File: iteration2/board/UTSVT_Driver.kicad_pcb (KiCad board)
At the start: 2 copper layers, 23 parts

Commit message: Generated netlist
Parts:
- added C1: C, Capacitors_SMD:C_0805_HandSoldering, F.Cu at (142.3, 2.73)
- added C2: 100nF, Capacitors_SMD:C_0805_HandSoldering, F.Cu at (151.3, 9.78)
- added C3: 100nF, Capacitors_SMD:C_0805_HandSoldering, F.Cu at (151.3, 25.8)
- added C4: 100nF, Capacitors_SMD:C_0805_HandSoldering, F.Cu at (151.3, 41.8)
- added C5: 100nF, Capacitors_SMD:C_0805_HandSoldering, F.Cu at (151.3, 50.7)
- added D1: BAV99, Diodes_SMD:D_0805, F.Cu at (162.6, 8.07)
- added D2: BAV99, Diodes_SMD:D_0805, F.Cu at (162.6, 24.1)
- added D3: BAV99, Diodes_SMD:D_0805, F.Cu at (162.6, 40.1)
- added D4: BAV99, Diodes_SMD:D_0805, F.Cu at (161.4, 50.6)
- added J1: DB37_Female_MountingHoles, Connectors_DSub:DB37FC, F.Cu at (9.22, 20.9)
- added Q1: 2N7002, TO_SOT_Packages_SMD:SOT-23, F.Cu at (151.9, 3.48)
- added Q2: 2N7002, TO_SOT_Packages_SMD:SOT-23, F.Cu at (151.9, 19.5)
- added Q3: 2N7002, TO_SOT_Packages_SMD:SOT-23, F.Cu at (151.9, 35.5)
- added R1: 10K, Resistors_SMD:R_0805_HandSoldering, F.Cu at (157.5, 8.18)
- added R10: 10K, Resistors_SMD:R_0805_HandSoldering, F.Cu at (151.3, 56.2)
- added R11: 1M, Resistors_SMD:R_0805_HandSoldering, F.Cu at (156.3, 50.7)
- added R2: 10K, Resistors_SMD:R_0805_HandSoldering, F.Cu at (162.7, 2.67)
- added R3: 10K, Resistors_SMD:R_0805_HandSoldering, F.Cu at (157.5, 2.67)
- added R4: 10K, Resistors_SMD:R_0805_HandSoldering, F.Cu at (157.5, 24.2)
- added R5: 10K, Resistors_SMD:R_0805_HandSoldering, F.Cu at (162.7, 18.7)
- added R6: 10K, Resistors_SMD:R_0805_HandSoldering, F.Cu at (157.5, 18.7)
- added R7: 10K, Resistors_SMD:R_0805_HandSoldering, F.Cu at (157.5, 34.7)
- added R8: 10K, Resistors_SMD:R_0805_HandSoldering, F.Cu at (162.7, 34.7)
- added R9: 10K, Resistors_SMD:R_0805_HandSoldering, F.Cu at (157.5, 40.2)
- added U1: Nucleo, UTSVT_board:AFBShieldBoard, F.Cu at (17.5, 53.4)
- added U2: SN65HVD230, Housings_SOIC:SOIC-8_3.9x4.9mm_Pitch1.27mm, F.Cu at (97.1, 57.3)
- added U3: CAN_adapter, UTSVT_board:CAN_adapter, F.Cu at (59.5, 31.8)
- moved REF** 111.0 mm to (7.50, 78.7)
- moved REF** 93.1 mm to (25.0, 78.7)
- moved REF** 78.9 mm to (57.7, 40.6)
- moved REF** 70.3 mm to (128.5, 17.4)
- moved REF** 65.9 mm to (57.7, 46.1)
- moved REF** 65.7 mm to (122.7, 22.8)
- moved REF** 64.0 mm to (122.7, 28.2)
- moved REF** 63.5 mm to (42.6, 78.7)
- moved REF** 63.4 mm to (57.7, 64.6)
- moved REF** 63.4 mm to (140.2, 17.3)
- moved REF** 62.1 mm to (128.7, 28.2)
- moved REF** 53.5 mm to (128.7, 22.8)
- moved REF** 52.3 mm to (57.7, 70.1)
- moved REF** 50.4 mm to (61.7, 57.3)
- moved REF** 49.2 mm to (130.3, 8.60)
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
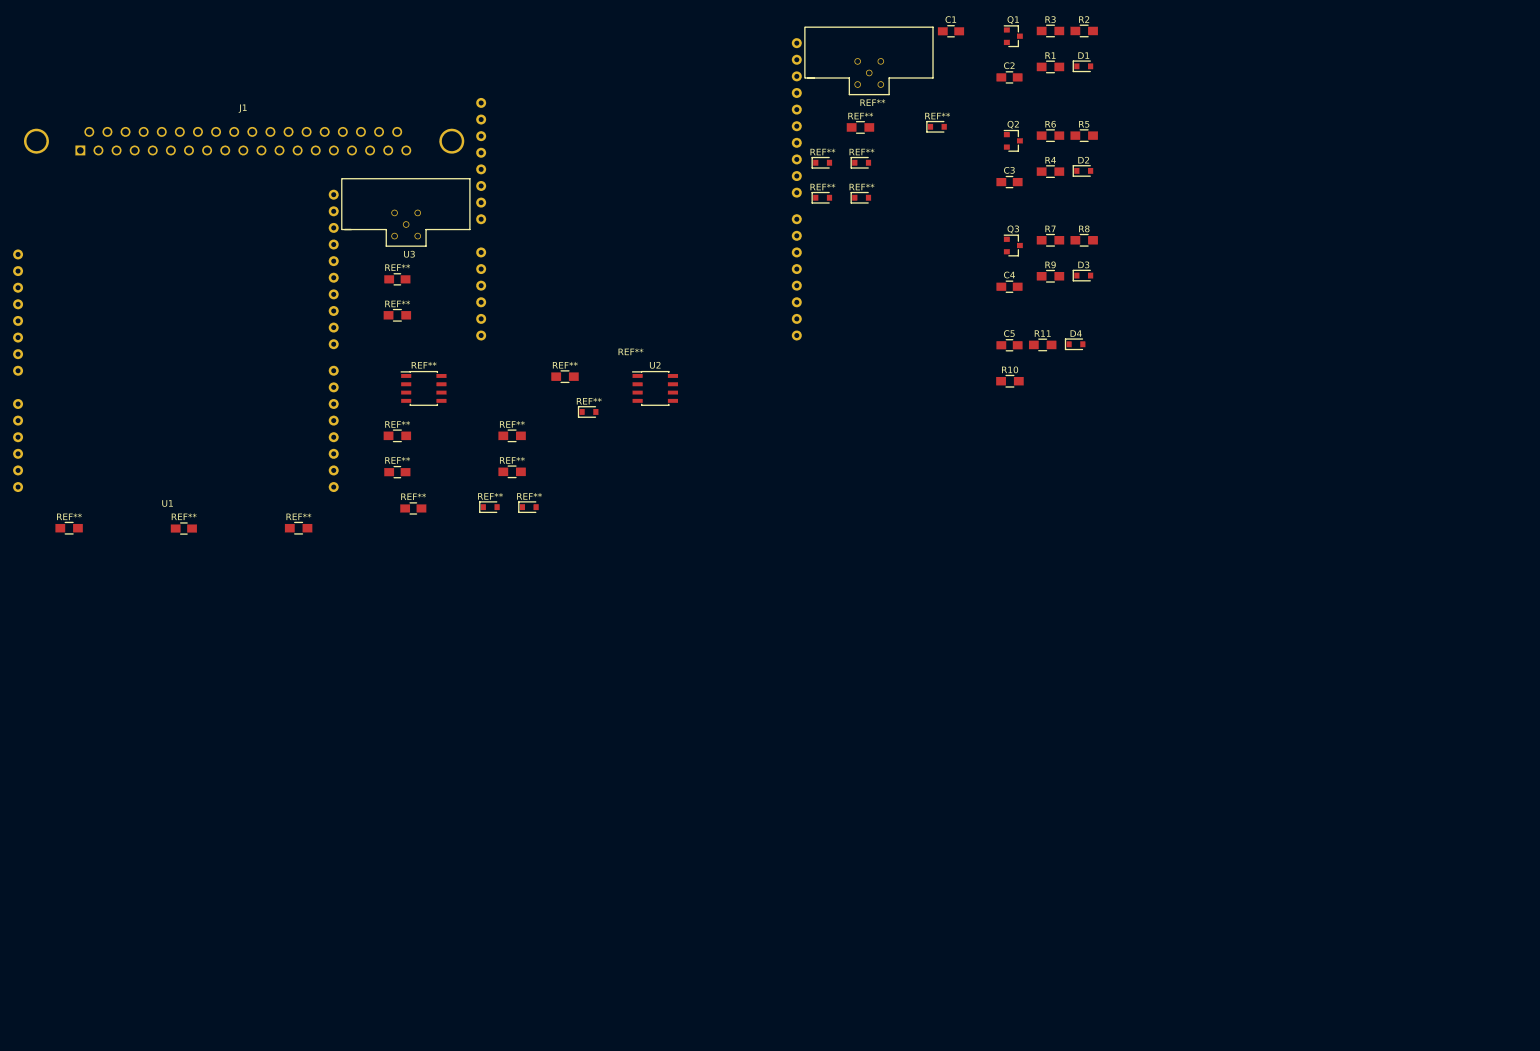
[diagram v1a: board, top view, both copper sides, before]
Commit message: Redid some components to fit footprint
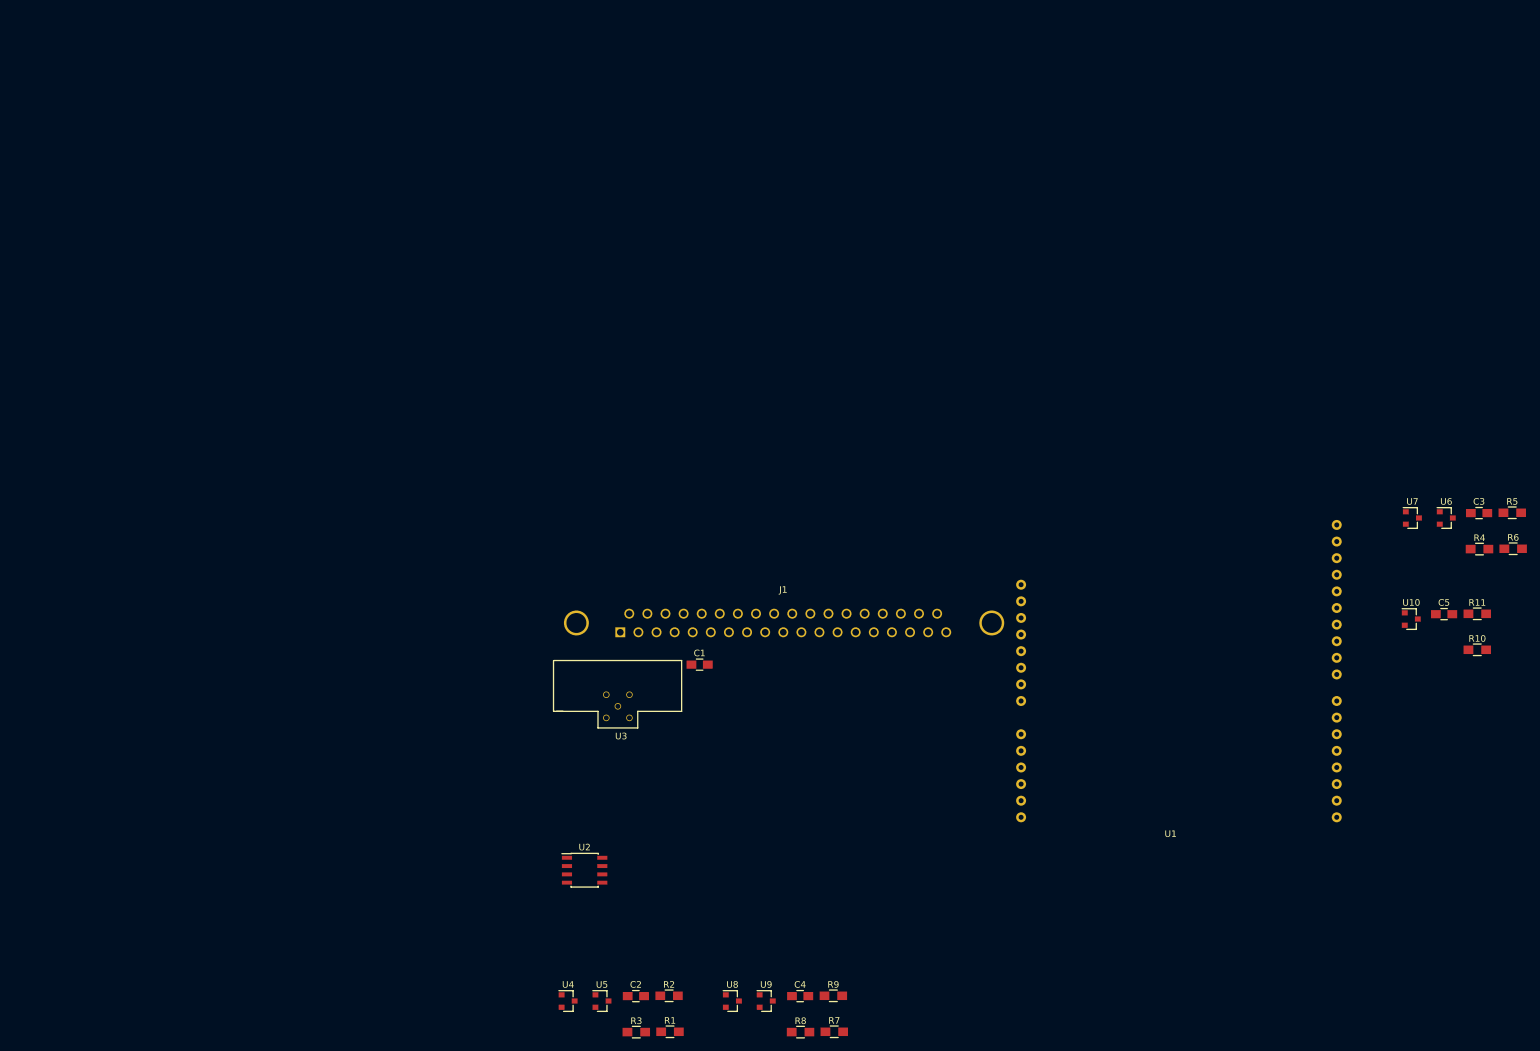
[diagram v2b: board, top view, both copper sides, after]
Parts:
- removed D1, D2, D3, D4: BAV99, Diodes_SMD:D_0805
- removed Q1, Q2, Q3: 2N7002, TO_SOT_Packages_SMD:SOT-23
- removed REF** (x8): R_0805_HandSoldering, Resistors_SMD:R_0805_HandSoldering
- removed REF** (x8): D_0805, Diodes_SMD:D_0805
- removed REF** (x4): C_0805_HandSoldering, Capacitors_SMD:C_0805_HandSoldering
- removed REF**: CANadapter, MotorControllerStuff:CANadapter
- removed REF**: SOIC-8_3.9x4.9mm_Pitch1.27mm, Housings_SOIC:SOIC-8_3.9x4.9mm_Pitch1.27mm
- removed REF**: AFBShield Board, MotorControllerStuff:AFBShieldBoard
- added U10: BAV99, TO_SOT_Packages_SMD:SOT-23, F.Cu at (212.7, 92.6)
- added U4: BAV99, TO_SOT_Packages_SMD:SOT-23, F.Cu at (83.8, 151.0)
- added U5: MOS_N, TO_SOT_Packages_SMD:SOT-23, F.Cu at (89.0, 151.0)
- added U6: BAV99, TO_SOT_Packages_SMD:SOT-23, F.Cu at (218.0, 77.1)
- added U7: MOS_N, TO_SOT_Packages_SMD:SOT-23, F.Cu at (212.9, 77.1)
- added U8: BAV99, TO_SOT_Packages_SMD:SOT-23, F.Cu at (108.9, 151.0)
- added U9: MOS_N, TO_SOT_Packages_SMD:SOT-23, F.Cu at (114.1, 151.0)
- J1: footprint Connectors_DSub:DB37FC -> UTSVT_board:DB37FC
- moved R3 165.6 mm to (94.2, 155.7)
- moved U1 161.4 mm to (170.8, 103.8)
- moved R2 160.6 mm to (99.2, 150.2)
- moved R1 158.6 mm to (99.4, 155.7)
- moved C2 151.6 mm to (94.1, 150.2)
- moved R8 128.6 mm to (119.3, 155.7)
- moved R7 125.4 mm to (124.5, 155.7)
- moved R9 114.9 mm to (124.3, 150.2)
- moved C4 113.1 mm to (119.3, 150.2)
- moved J1 110.6 mm to (91.8, 94.6)
- moved C1 104.2 mm to (103.9, 99.6)
- moved R6 94.8 mm to (228.3, 81.8)
- moved C3 87.8 mm to (223.1, 76.4)
- moved R4 87.4 mm to (223.1, 81.9)
- moved R5 87.2 mm to (228.1, 76.3)
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
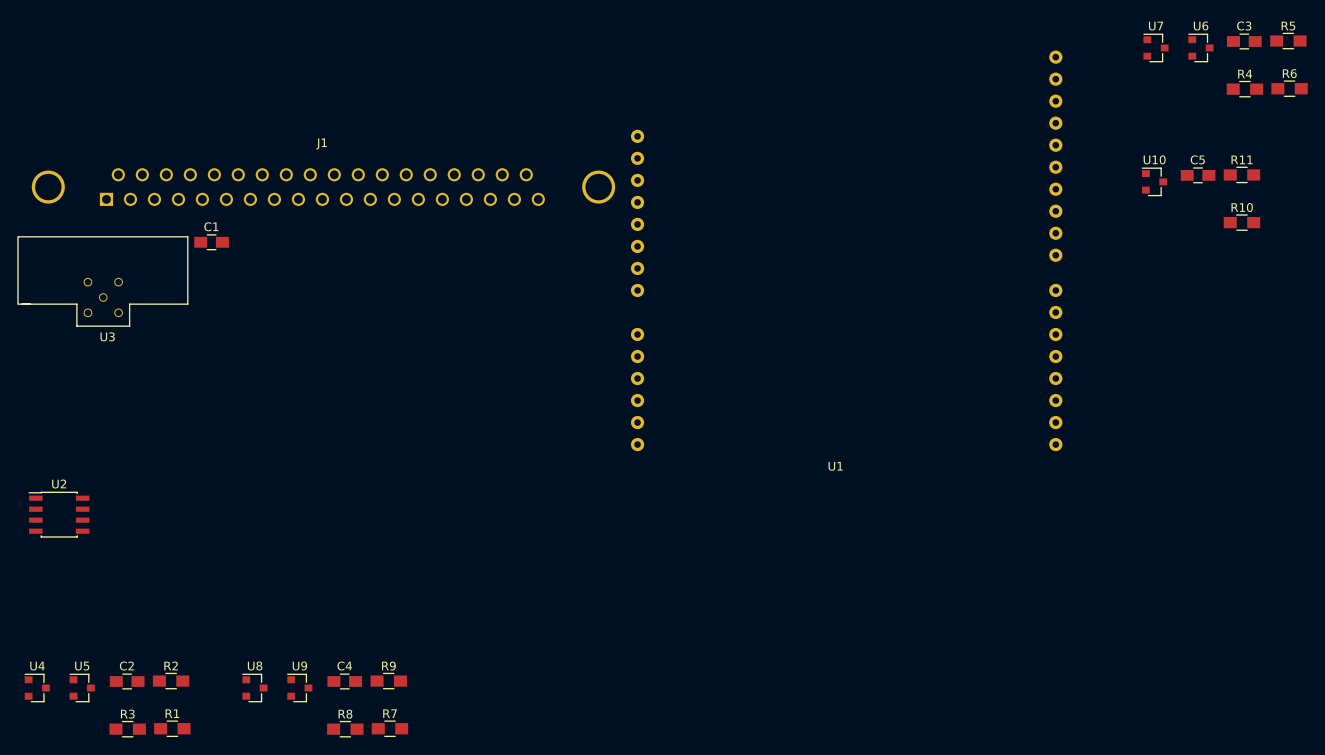
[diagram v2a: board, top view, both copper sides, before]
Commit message: partially resolved merge issues and added script for automatic merging
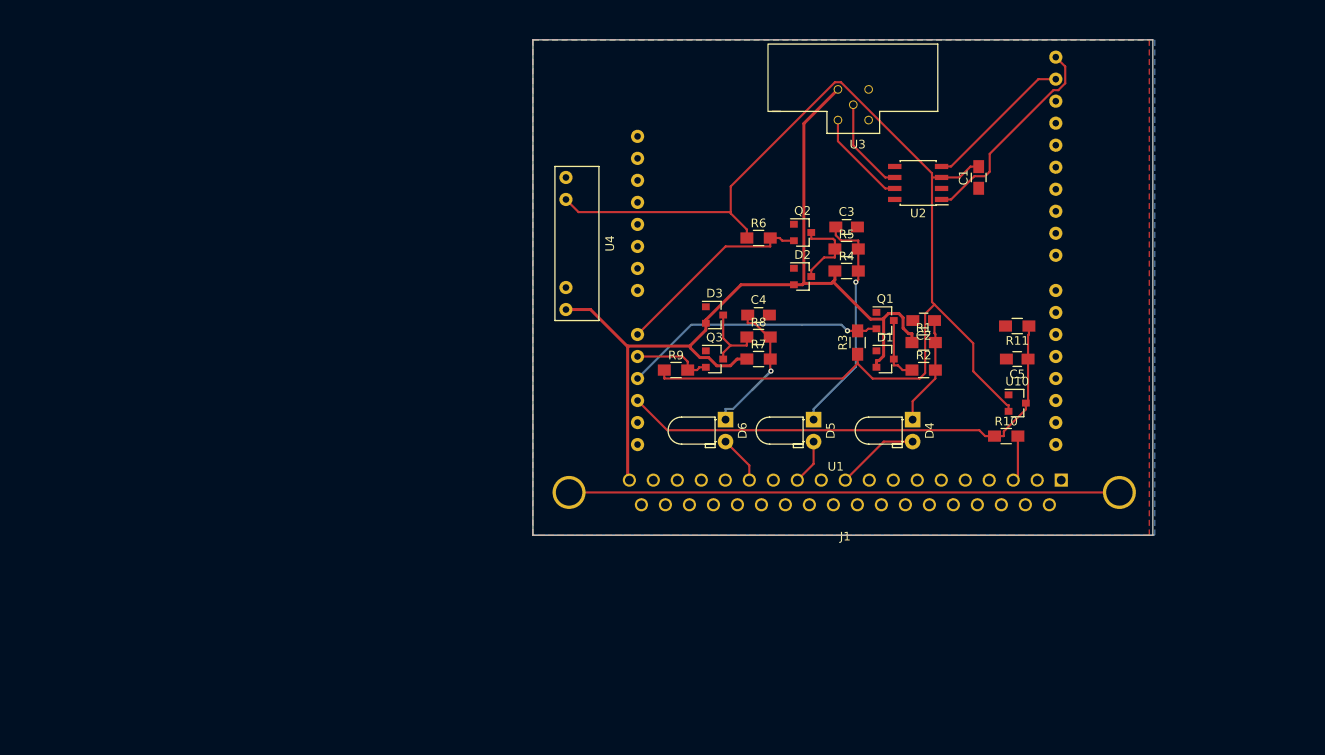
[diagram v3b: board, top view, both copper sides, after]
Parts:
- removed U5, U7, U9: MOS_N, TO_SOT_Packages_SMD:SOT-23
- removed U6, U8: BAV99, TO_SOT_Packages_SMD:SOT-23
- added D1: BAV99, TO_SOT_Packages_SMD:SOT-23, F.Cu at (181.6, 113.0)
- added D2: BAV99, TO_SOT_Packages_SMD:SOT-23, F.Cu at (172.1, 103.5)
- added D3: BAV99, TO_SOT_Packages_SMD:SOT-23, F.Cu at (161.9, 108.0)
- added D4: LED, LEDs:LED_D3.0mm_Horizontal_O1.27mm_Z10.0mm, F.Cu at (184.8, 120.0)
- added D5: LED, LEDs:LED_D3.0mm_Horizontal_O1.27mm_Z10.0mm, F.Cu at (173.4, 120.0)
- added D6: LED, LEDs:LED_D3.0mm_Horizontal_O1.27mm_Z10.0mm, F.Cu at (163.2, 120.0)
- added Q1: 2N7002, TO_SOT_Packages_SMD:SOT-23, F.Cu at (181.6, 108.6)
- added Q2: 2N7002, TO_SOT_Packages_SMD:SOT-23, F.Cu at (172.1, 98.4)
- added Q3: 2N7002, TO_SOT_Packages_SMD:SOT-23, F.Cu at (161.9, 113.0)
- U4: value BAV99 -> REM1_12to3.3; footprint TO_SOT_Packages_SMD:SOT-23 -> MotorControllerStuff:REM1_12to3.3
- moved J1 114.8 mm to (201.9, 127.0), turned to 180 degrees
- moved U2 106.2 mm to (185.4, 92.7), turned to 180 degrees
- moved C2 100.9 mm to (186.1, 108.6), turned to 180 degrees
- moved R1 97.5 mm to (186.1, 111.1)
- moved R3 95.3 mm to (178.4, 111.1), turned to 90 degrees
- moved R2 94.0 mm to (186.1, 114.3)
- moved U3 89.4 mm to (178.4, 83.2)
- moved C1 88.8 mm to (192.4, 92.1), turned to 90 degrees
- moved U4 79.7 mm to (144.8, 99.7), turned to 90 degrees
- moved R8 65.7 mm to (167.0, 110.5)
- moved C4 63.8 mm to (167.0, 108.0)
- moved R6 63.6 mm to (167.0, 99.1)
- moved R7 60.2 mm to (167.0, 113.0)
- moved R5 56.3 mm to (177.2, 100.3)
- moved C3 50.6 mm to (177.2, 97.8)
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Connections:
- C1 pad 2: +3V3 -> 3.3V
- J1 pad 10: /step_down_circuit1/Vin -> Net-(D4-Pad2)
- J1 pad 12: /step_down_circuit2/Vin -> Net-(D5-Pad2)
- J1 pad 14: /step_down_circuit3/Vin -> Net-(D6-Pad2)
- J1 pad 19: Net-(J1-Pad19) -> +12V
- R2 pad 1: Net-(R2-Pad1) -> Net-(D1-Pad3)
- R3 pad 1: +3.3V -> 3.3V
- R6 pad 1: +3.3V -> 3.3V
- R9 pad 1: +3.3V -> 3.3V
- U1 pad 10: /step_down_circuit2/Vout -> /step_down_circuit3/Vout
- U1 pad 11: /step_down_circuit3/Vout -> /step_down_circuit1/Vout
- U1 pad 9: /step_down_circuit1/Vout -> /step_down_circuit2/Vout
- U10 pad 2: +3.3V -> 3.3V
- U2 pad 3: +3V3 -> 3.3V
- U3 pad 2: VCC -> +12V
- U4 pad 1: GND -> +12V
- U4 pad 2: +12V -> GND
- U4 pad 3: Net-(R2-Pad1) -> 3.3V
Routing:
- net 3.3V: track 0.00 -> 138.2 mm
- net +12V: track 0.00 -> 105.1 mm
- net Net-(J1-Pad0): track 0.00 -> 63.5 mm
- net /step_down_circuit_analog1/Vout: track 0.00 -> 58.2 mm
- net /step_down_circuit1/Vout: track 0.00 -> 30.5 mm, vias 0 -> 1
- net /step_down_circuit2/Vin: track 0.00 -> 26.6 mm, vias 0 -> 1
- net Net-(U1-Pad15): track 0.00 -> 24.5 mm
- net /step_down_circuit2/Vout: track 0.00 -> 23.4 mm
- net /step_down_circuit3/Vin: track 0.00 -> 19.6 mm, vias 0 -> 1
- net Net-(U1-Pad16): track 0.00 -> 17.4 mm
- net /step_down_circuit1/Vin: track 0.00 -> 12.6 mm
- net Net-(U2-Pad7): track 0.00 -> 11.2 mm
- net Net-(U2-Pad6): track 0.00 -> 11.0 mm
- net Net-(D4-Pad2): track 0.00 -> 9.62 mm
- net Net-(D2-Pad3): track 0.00 -> 9.56 mm
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- added copper zone on B.Cu, net GND
- added copper zone on F.Cu, net GND
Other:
- board outline added: 71.5 x 57.1 mm
- net class Power12 added: clearance 0.2, trace_width 0.35, via_dia 0.6, via_drill 0.4
